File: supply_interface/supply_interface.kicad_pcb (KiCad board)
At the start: 2 copper layers, 93 x 152 mm, 22 parts, among them J1 39-28-1243, J10 MBES-152, J11 MBES-152, J12 MBES-152, J13 MBES-152, J2 39-28-1043, J3 MBES-152, J4 MBES-152, J5 282837-3, J6 MBES-152, J7 39-28-1043, J8 MBES-152, J9 MBES-152

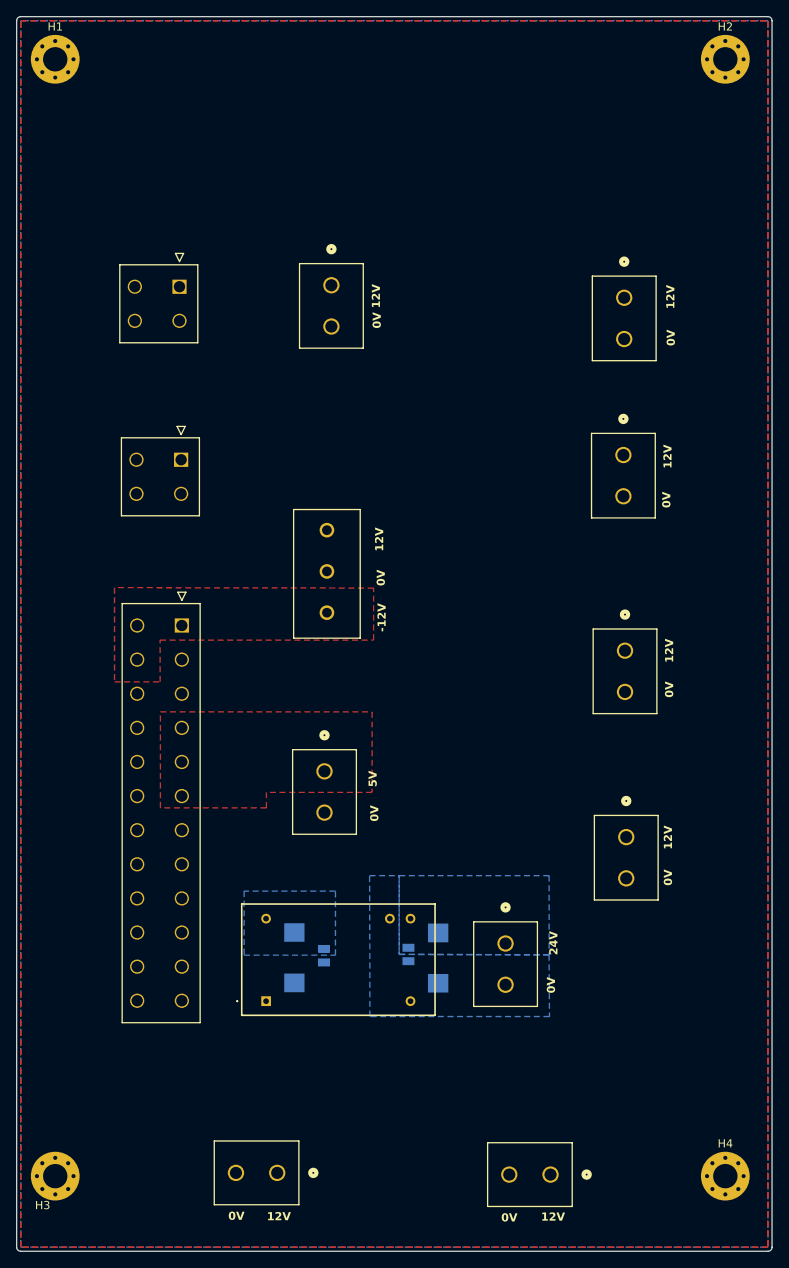
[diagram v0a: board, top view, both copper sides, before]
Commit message: Update supply interface
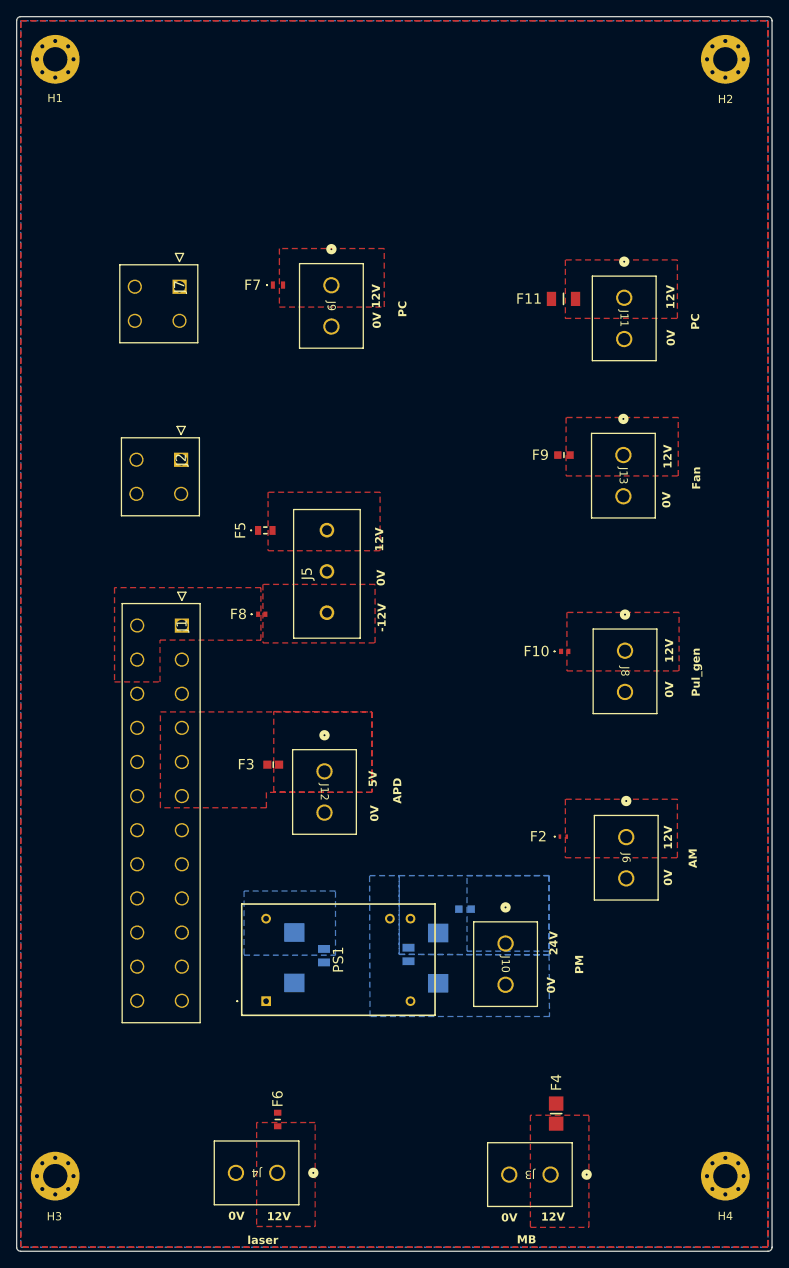
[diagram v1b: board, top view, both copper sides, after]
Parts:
- added F1: SF-0603FP080-2, vq:FUSC1608X55N, B.Cu at (95.5, 134.6)
- added F10: 0ABA-0200-TN, vq:0ABA0200TN, F.Cu at (107.7, 102.9)
- added F11: 0501015.WRA, vq:FUSC3216X98N, F.Cu at (107.6, 59.5)
- added F2: F0402G0R10FNTR, vq:F0402G0R10FNTR, F.Cu at (107.5, 125.7)
- added F3: 043802.5WRA, vq:FUSC1608X61N, F.Cu at (71.8, 116.8)
- added F4: 0483010.DR, vq:FUSC3316X137N, F.Cu at (106.7, 159.8)
- added F5: 049401.5NRHF, vq:0494015NRHF, F.Cu at (70.9, 88.0)
- added F6: 0494002.NRHF, vq:FUSC1608X30N, F.Cu at (72.4, 160.5)
- added F7: 0ABB-8000-TM, vq:0ABB8000TM, F.Cu at (72.4, 57.8)
- added F8: 0ABA-0200-TN, vq:0ABA0200TN, F.Cu at (70.4, 98.3)
- added F9: SF-0603SP080-2, vq:FUSC1608X55N, F.Cu at (107.6, 78.7)
- C1, C2: footprint mes_empreintes:CAPPM7343X310N -> vq:CAPPM7343X310N
- C3, C4: footprint mes_empreintes:CAPC2012X145N -> vq:CAPC2012X145N
- J1: footprint mes_empreintes:39-28-1243 -> vq:39-28-1243
- J10, J11, J12, J13, J3, J4, J6, J8, J9: footprint mes_empreintes:CONN_MBES-152_ALT -> vq:CONN_MBES-152_ALT
- J2, J7: footprint mes_empreintes:39-28-1043 -> vq:39-28-1043
- J5: footprint mes_empreintes:2828373 -> vq:2828373
- PS1: footprint mes_empreintes:TEL151215N -> vq:TEL151215N
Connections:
- J10 pad 1: 24 V -> /pm
- J11 pad 1: 12V -> /pc
- J12 pad 1: 5V -> /apd
- J13 pad 1: 12V -> /fan
- J3 pad 1: 12V -> /MB
- J4 pad 1: 12V -> /laser
- J5 pad 1: -12V -> /pol_n
- J5 pad 3: 12V -> /pol_p
- J6 pad 1: 12V -> /am
- J8 pad 1: 12V -> /pulse_gen
- J9 pad 1: 12V -> /peltier
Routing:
- added copper zone on F.Cu, net /MB
- added copper zone on F.Cu, net /am
- added copper zone on F.Cu, net /apd
- added copper zone on F.Cu, net /fan
- added copper zone on F.Cu, net /laser
- added copper zone on F.Cu, net /pc
- added copper zone on F.Cu, net /peltier
- added copper zone on B.Cu, net /pm
- added copper zone on F.Cu, net /pol_n
- added copper zone on F.Cu, net /pol_p
- added copper zone on F.Cu, net /pulse_gen
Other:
- board text added: "AM"
- board text added: "APD"
- board text added: "Fan"
- board text added: "MB"
- board text added: "PC"
- board text added: "PM"
- board text added: "Pul_gen"
- board text added: "laser"

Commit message: Add TVS protection and decoupling capacitors for power rails
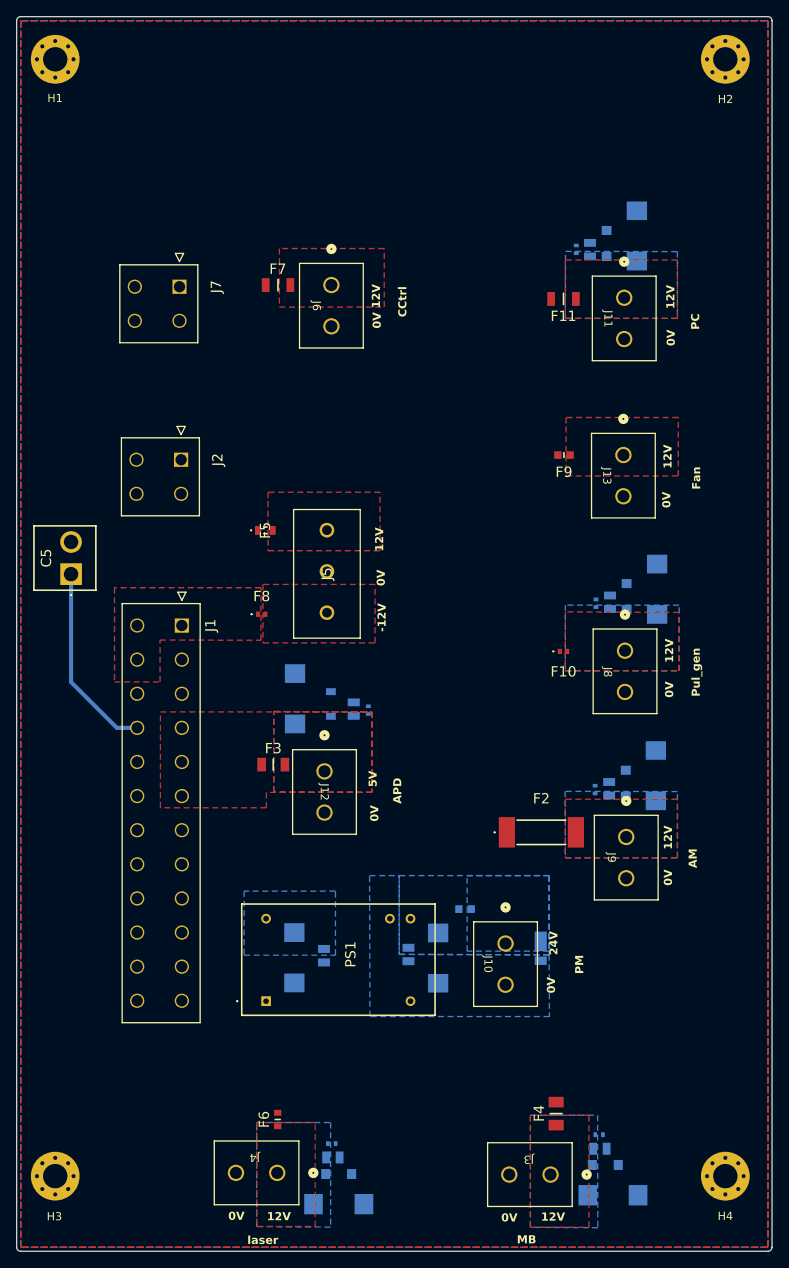
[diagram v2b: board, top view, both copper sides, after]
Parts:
- added C10: 22 uF, vq:CAPC2012X145N, B.Cu at (113.3, 96.8)
- added C11: 100 uF, vq:CAPPM7343X310N, B.Cu at (119.1, 95.2)
- added C12: 1 uF, vq:GRM15x, B.Cu at (79.0, 163.5)
- added C13: 22 uF, vq:CAPC2012X145N, B.Cu at (79.2, 165.2)
- added C14: 100 uF, vq:CAPPM7343X310N, B.Cu at (79.9, 170.9)
- added C15: 1 uF, vq:GRM15x, B.Cu at (112.0, 162.4)
- added C16: 22 uF, vq:CAPC2012X145N, B.Cu at (112.1, 164.1)
- added C17: 100 uF, vq:CAPPM7343X310N, B.Cu at (113.7, 169.8)
- added C18: 1 uF, vq:GRM15x, B.Cu at (111.5, 119.9)
- added C19: 22 uF, vq:CAPC2012X145N, B.Cu at (113.2, 119.8)
- added C20: 100 uF, vq:CAPPM7343X310N, B.Cu at (119.0, 118.2)
- added C21: 1 uF, vq:GRM15x, B.Cu at (109.1, 53.4)
- added C22: 22 uF, vq:CAPC2012X145N, B.Cu at (110.8, 53.4)
- added C23: 100 uF, vq:CAPPM7343X310N, B.Cu at (116.6, 51.7)
- added C24: 1 uF, vq:GRM15x, B.Cu at (83.5, 110.1)
- added C25: 22 uF, vq:CAPC2012X145N, B.Cu at (81.8, 110.0)
- added C26: 100 uF, vq:CAPPM7343X310N, B.Cu at (74.5, 108.7)
- added C5: 1744002-2, vq:17440022, F.Cu at (47.0, 93.4)
- added C9: 1 uF, vq:GRM15x, B.Cu at (111.6, 97.0)
- added D1: TVS 12V, vq:SODFL3718X130N, B.Cu at (115.3, 96.2)
- added D2: TVS 12V, vq:SODFL3718X130N, B.Cu at (79.9, 167.2)
- added D3: TVS 12V, vq:SODFL3718X130N, B.Cu at (112.7, 166.1)
- added D4: TVS 12V, vq:SODFL3718X130N, B.Cu at (115.2, 119.1)
- added D5: TVS 12V, vq:SODFL3718X130N, B.Cu at (112.9, 52.7)
- added D6: SMF6V0TR, vq:SMF6V0TR, B.Cu at (79.0, 109.4)
- added D7: DFLT27A-7, vq:DFLT27A7, B.Cu at (104.8, 139.4)
- F1: value SF-0603FP080-2 -> SF-0603S100-2
- F11: value 0501015.WRA -> 3413.0329.22; footprint vq:FUSC3216X98N -> vq:FUSC3216X60N
- F2: value F0402G0R10FNTR -> 3403.0157.24; footprint vq:F0402G0R10FNTR -> vq:3403015724
- F3: value 043802.5WRA -> SF-1206S300-2; footprint vq:FUSC1608X61N -> vq:FUSC3116X70N
- F4: value 0483010.DR -> SF-1206S1000R-2; footprint vq:FUSC3316X137N -> vq:FUSC3216X90N
- F7: value 0ABB-8000-TM -> 3413.0329.22; footprint vq:0ABB8000TM -> vq:FUSC3216X60N
- moved J6 77.1 mm to (79.0, 57.8)
- moved J9 77.0 mm to (115.3, 125.7)
- moved F2 2.75 mm to (104.8, 125.2)
- moved F10 0.15 mm to (107.6, 102.9)
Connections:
- J1 pad 16: unconnected-(J1-Pad16) -> Net-(C5-Pad1)
- J3 pad 2: GND -> unconnected-(J3-Pad2)
- J6 pad 1: /am -> /peltier
- J9 pad 1: /peltier -> /am
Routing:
- net Net-(C5-Pad1): track 0.00 -> 23.8 mm
- added copper zone on B.Cu, net /MB
- added copper zone on B.Cu, net /am
- added copper zone on B.Cu, net /apd
- added copper zone on B.Cu, net /laser
- added copper zone on B.Cu, net /pc
- added copper zone on B.Cu, net /pulse_gen
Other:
- board text added: "CCtrl"

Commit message: update2 ps_on connector
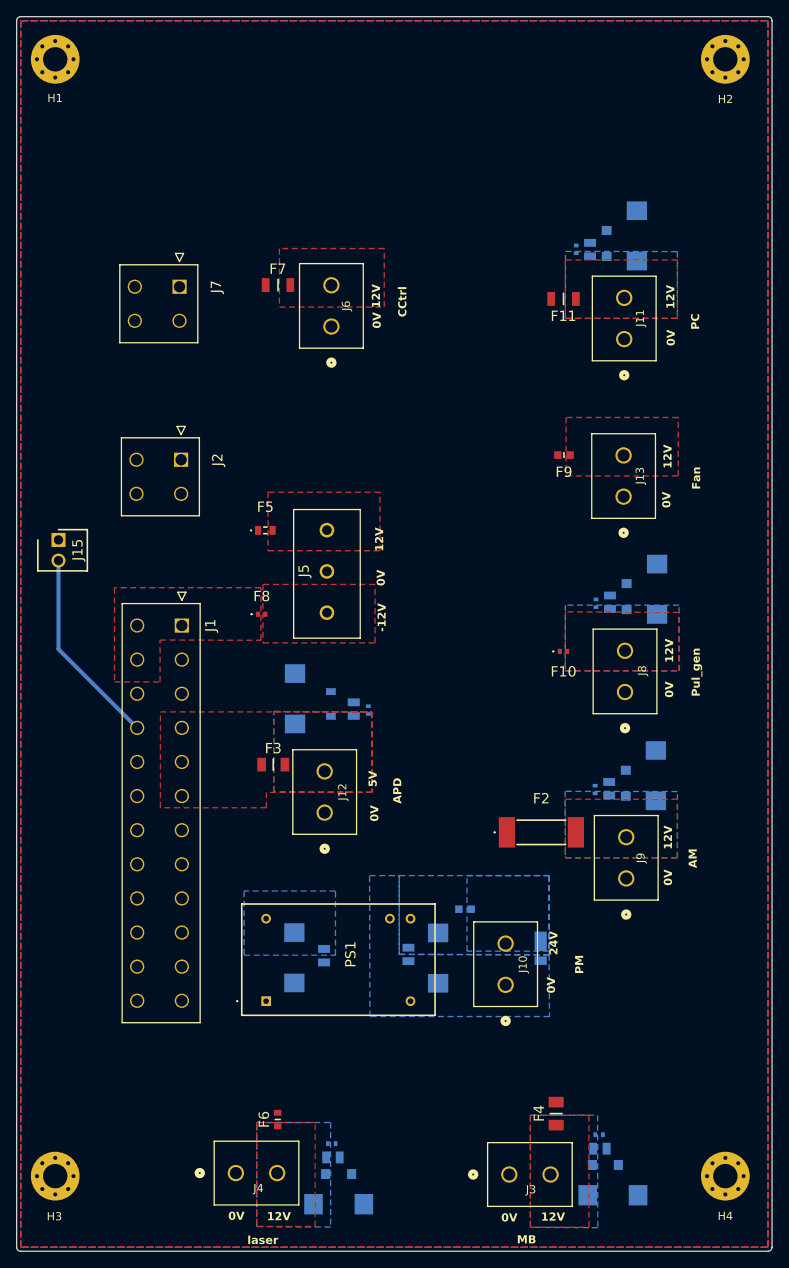
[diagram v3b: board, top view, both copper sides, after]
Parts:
- removed C5: 1744002-2, vq:17440022
- added J15: 3-641215-2, vq:SHDR2W66P0X254_1X2_508X572X813P, F.Cu at (45.4, 89.2)
- moved J13 5.13 mm to (115.0, 83.8), turned to 90 degrees
- moved J6 5.10 mm to (79.0, 62.9), turned to 90 degrees
- moved J9 5.10 mm to (115.3, 130.8), turned to 90 degrees
- moved J4 5.09 mm to (67.2, 167.1), turned to 0 degrees
- moved J10 5.09 mm to (100.5, 143.9), turned to 90 degrees
- moved J11 5.09 mm to (115.0, 64.5), turned to 90 degrees
- moved J8 5.09 mm to (115.2, 107.9), turned to 90 degrees
- moved J12 5.09 mm to (78.2, 122.8), turned to 90 degrees
- moved J3 5.08 mm to (100.9, 167.3), turned to 0 degrees
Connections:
- J10 pad 1: /pm -> 0 V
- J10 pad 2: 0 V -> /pm
- J11 pad 1: /pc -> GND
- J11 pad 2: GND -> /pc
- J12 pad 1: /apd -> GND
- J12 pad 2: GND -> /apd
- J13 pad 1: /fan -> GND
- J13 pad 2: GND -> /fan
- J3 pad 1: /MB -> GND
- J3 pad 2: unconnected-(J3-Pad2) -> /MB
- J4 pad 1: /laser -> GND
- J4 pad 2: GND -> /laser
- J6 pad 1: /peltier -> GND
- J6 pad 2: GND -> /peltier
- J8 pad 1: /pulse_gen -> GND
- J8 pad 2: GND -> /pulse_gen
- J9 pad 1: /am -> GND
- J9 pad 2: GND -> /am
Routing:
- net Net-(J1-Pad16): track 23.8 -> 24.6 mm
